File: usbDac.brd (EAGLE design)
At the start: 37 x 12.1 mm, 26 parts, among them X1 USBPCB

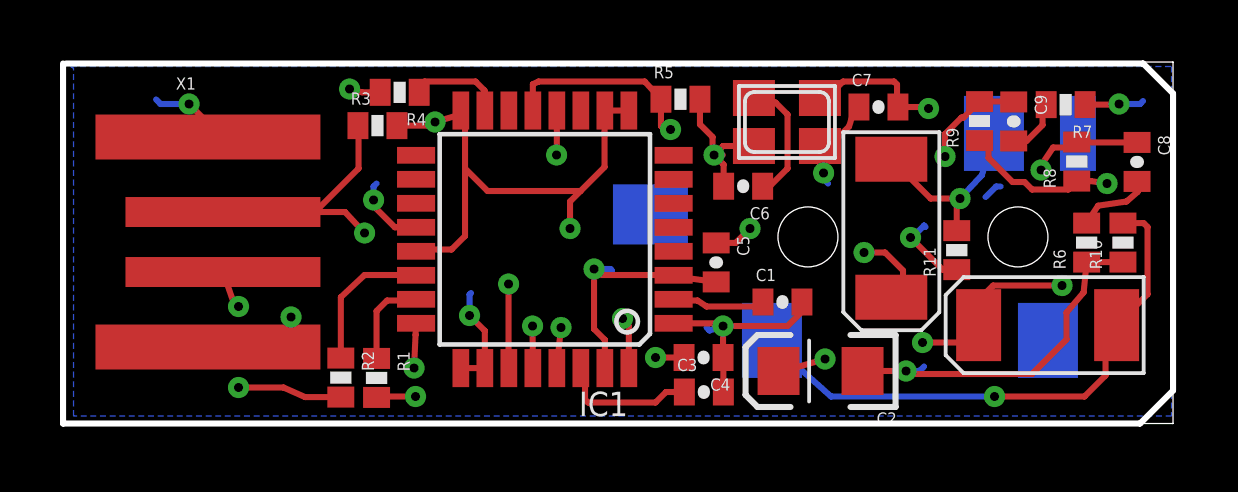
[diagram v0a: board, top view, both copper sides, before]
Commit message: had to make it 2-layer cause 4-layer is 5x more expensive :(
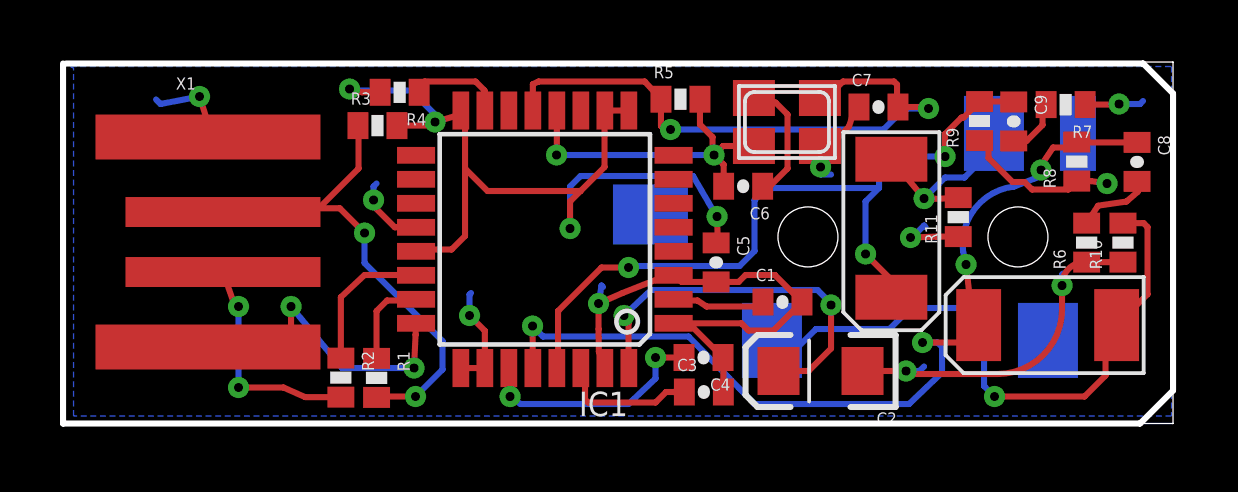
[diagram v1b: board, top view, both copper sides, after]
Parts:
- moved R11 1.10 mm to (29.8, 6.88)
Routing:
- net N$12: track 23.1 -> 26.4 mm
- net N$4: track 11.2 -> 8.10 mm
- net N$8: track 19.7 -> 16.9 mm
- net N$18: track 18.7 -> 21.3 mm
- net GND: track 50.5 -> 51.9 mm
- net N$14: track 30.7 -> 31.7 mm
- net VDD: track 29.5 -> 30.4 mm
- net VCC: track 10.1 -> 10.7 mm
- net N$3: track 12.2 -> 12.8 mm
